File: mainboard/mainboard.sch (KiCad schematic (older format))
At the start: 96 parts, among them J1 USB_B_Micro, J2 Conn_01x19_MountingPin, J3 Conn_01x19_MountingPin, J4 Conn_01x02_Male, Q1 DMG2301L, Q2 MMBT3904, Q3 MMBT3904, SW1 SW_Push, SW2 SW_Push, U1 ESP32-WROOM-32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

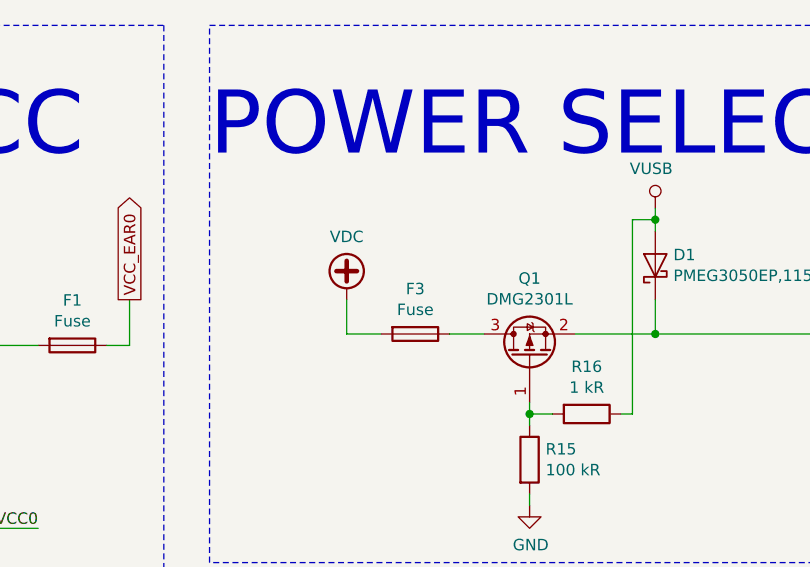
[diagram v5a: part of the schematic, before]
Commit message: Add right-angle XT30 power connector
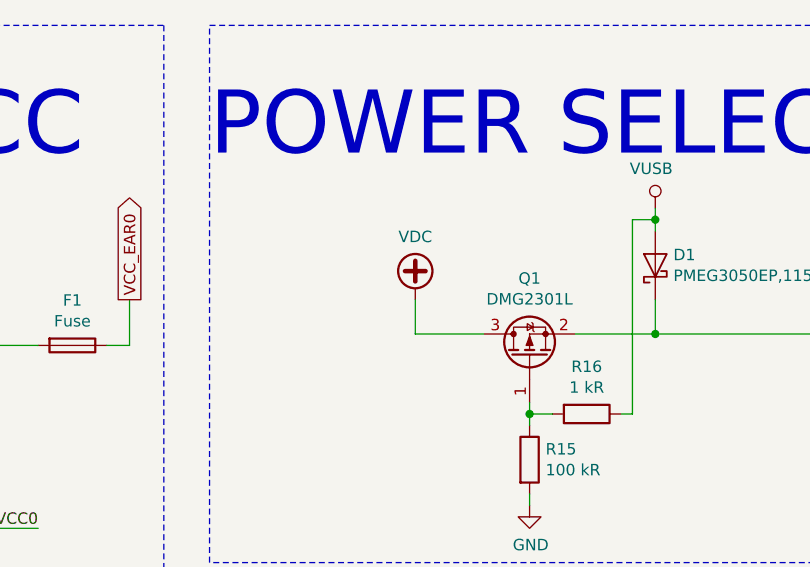
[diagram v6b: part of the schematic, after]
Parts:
- removed F3: Fuse, Fuse:Fuse_0805_2012Metric, symbol Device:Fuse
- F4: footprint Fuse:Fuse_0805_2012Metric -> Fuse:Fuse_1206_3216Metric
- J4: footprint (none) -> mainboard:XT30PW
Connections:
- net VDC: now also Q1.3 (D)
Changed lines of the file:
@@
 L power:VDC #PWR0119
 U 1 1 5D52A44C
-P 7450 5100
-F 0 "#PWR0119" H 7450 5000 50  0001 C CNN
-F 1 "VDC" H 7450 5375 50  0000 C CNN
-F 2 "" H 7450 5100 50  0001 C CNN
-F 3 "" H 7450 5100 50  0001 C CNN
-	1    7450 5100
+P 7750 5100
+F 0 "#PWR0119" H 7750 5000 50  0001 C CNN
+F 1 "VDC" H 7750 5375 50  0000 C CNN
+F 2 "" H 7750 5100 50  0001 C CNN
+F 3 "" H 7750 5100 50  0001 C CNN
+	1    7750 5100
 	1    0    0    -1
 $EndComp
@@
 Wire Wire Line
 	7000 7350 7350 7350
-$Comp
-L Device:Fuse F3
-U 1 1 5EE0ACB2
-P 7750 5250
-F 0 "F3" V 7553 5250 50  0000 C CNN
-F 1 "Fuse" V 7644 5250 50  0000 C CNN
-F 2 "Fuse:Fuse_0805_2012Metric" V 7680 5250 50  0001 C CNN
-F 3 "~" H 7750 5250 50  0001 C CNN
-	1    7750 5250
-	0    1    1    0
-$EndComp
-Wire Wire Line
-	7900 5250 8050 5250
-Wire Wire Line
-	7450 5100 7450 5250
-Wire Wire Line
-	7450 5250 7600 5250
+Wire Wire Line
+	7750 5100 7750 5250
 Wire Wire Line
 	17600 1950 17600 2250
@@
 F 0 "F4" V 14103 4750 50  0000 C CNN
 F 1 "Fuse" V 14194 4750 50  0000 C CNN
-F 2 "Fuse:Fuse_0805_2012Metric" V 14230 4750 50  0001 C CNN
+F 2 "Fuse:Fuse_1206_3216Metric" V 14230 4750 50  0001 C CNN
 F 3 "~" H 14300 4750 50  0001 C CNN
 	1    14300 4750
@@
 F 0 "J4" H 13858 4931 50  0000 C CNN
 F 1 "Conn_01x02_Male" H 13858 4840 50  0000 C CNN
-F 2 "" H 13750 4750 50  0001 C CNN
+F 2 "mainboard:XT30PW" H 13750 4750 50  0001 C CNN
 F 3 "~" H 13750 4750 50  0001 C CNN
 	1    13750 4750
@@
 Text Notes 13700 4300 0    276  ~ 0
 VDC
+Wire Wire Line
+	7750 5250 8050 5250
 Wire Bus Line
 	8350 2150 8350 2500

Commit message: More WIP
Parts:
- removed JP1, JP2, JP3: Jumper_3_Bridged12, Jumper:SolderJumper-3_P1.3mm_Bridged12_Pad1.0x1.5mm, symbol Jumper:Jumper_3_Bridged12
- added C44: 1 uC, Capacitor_SMD:C_0805_2012Metric, symbol Device:C
- added D3, D4, D5, D6, D7, D8, D9: LED, LED_SMD:LED_0805_2012Metric, symbol Device:LED
- added R23, R25: 1 kR, Resistor_SMD:R_0805_2012Metric, symbol Device:R
- added R24: 330 R, Resistor_SMD:R_0805_2012Metric, symbol Device:R
- added R26, R29: 220 R, Resistor_SMD:R_0805_2012Metric, symbol Device:R
- added R27, R28: 470 R, Resistor_SMD:R_0805_2012Metric, symbol Device:R
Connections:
- net +3V3: now also C44.1, D6.2 (A)
- net GND: now also U6.5 (SDO), U7.2 (ADDR), U8.9 (SDO/SA1), C44.2, R23.2, R24.2, R25.2, R26.2, R27.2, R28.2, R29.2
- net VBUS: now also D5.2 (A)
- net VCC_EAR0: now also D7.2 (A)
- net VCC_EAR1: now also D8.2 (A)
- net VDC: now also D3.2 (A)
- net VUSB: now also D4.2 (A)
- net IO4: now reaches U1.26 (IO4)
- net IO4: now also D9.2 (A)
- new net: D3.1 (K), R23.1
- new net: D4.1 (K), R24.1
- new net: D5.1 (K), R25.1
- new net: D6.1 (K), R26.1
- new net: D7.1 (K), R27.1
- new net: D8.1 (K), R28.1
- new net: D9.1 (K), R29.1
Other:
- note added: "LEDs"
- moved on the sheet: C41, C42, U8

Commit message: Finish basic routing
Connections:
- net +3V3: now also R26.1, U6.5 (SDO); no longer D6.2 (A)
- net GND: now also D5.1 (K), D6.1 (K); no longer R25.2, R26.2, U6.5 (SDO)
- net VBUS: now also R25.1; no longer D5.2 (A)
- new net: D5.2 (A), R25.2
- new net: D6.2 (A), R26.2
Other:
- moved on the sheet: D5, D6, R25, R26
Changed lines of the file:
@@
 	9200 10100 9200 9100
 Wire Wire Line
-	9200 9100 8200 9100
+	9200 9100 8800 9100
 Wire Wire Line
 	7250 10550 8000 10550
@@
 L Device:R R25
 U 1 1 5E59E276
-P 17300 4850
-F 0 "R25" H 17370 4896 50  0000 L CNN
-F 1 "1 kR" H 17370 4805 50  0000 L CNN
-F 2 "Resistor_SMD:R_0805_2012Metric" V 17230 4850 50  0001 C CNN
-F 3 "~" H 17300 4850 50  0001 C CNN
-	1    17300 4850
+P 17300 4500
+F 0 "R25" H 17370 4546 50  0000 L CNN
+F 1 "1 kR" H 17370 4455 50  0000 L CNN
+F 2 "Resistor_SMD:R_0805_2012Metric" V 17230 4500 50  0001 C CNN
+F 3 "~" H 17300 4500 50  0001 C CNN
+	1    17300 4500
 	1    0    0    -1
 $EndComp
@@
 F 3 "" H 17800 4200 50  0001 C CNN
 	1    17800 4200
-	1    0    0    -1
-$EndComp
-$Comp
-L Device:R R26
-U 1 1 5E5A0416
-P 17800 4850
-F 0 "R26" H 17870 4896 50  0000 L CNN
-F 1 "220 R" H 17870 4805 50  0000 L CNN
-F 2 "Resistor_SMD:R_0805_2012Metric" V 17730 4850 50  0001 C CNN
-F 3 "~" H 17800 4850 50  0001 C CNN
-	1    17800 4850
 	1    0    0    -1
 $EndComp
@@
 L Device:LED D5
 U 1 1 5E5A26C1
-P 17300 4500
-F 0 "D5" V 17339 4383 50  0000 R CNN
-F 1 "LED" V 17248 4383 50  0000 R CNN
-F 2 "LED_SMD:LED_0805_2012Metric" H 17300 4500 50  0001 C CNN
-F 3 "~" H 17300 4500 50  0001 C CNN
-	1    17300 4500
-	0    -1   -1   0
-$EndComp
-$Comp
-L Device:LED D6
-U 1 1 5E5A377A
-P 17800 4500
-F 0 "D6" V 17839 4383 50  0000 R CNN
-F 1 "LED" V 17748 4383 50  0000 R CNN
-F 2 "LED_SMD:LED_0805_2012Metric" H 17800 4500 50  0001 C CNN
-F 3 "~" H 17800 4500 50  0001 C CNN
-	1    17800 4500
+P 17300 4850
+F 0 "D5" V 17339 4733 50  0000 R CNN
+F 1 "LED" V 17248 4733 50  0000 R CNN
+F 2 "LED_SMD:LED_0805_2012Metric" H 17300 4850 50  0001 C CNN
+F 3 "~" H 17300 4850 50  0001 C CNN
+	1    17300 4850
 	0    -1   -1   0
 $EndComp
@@
 	8700 9500 8800 9500
 Wire Wire Line
-	8800 9500 8800 10550
-Wire Wire Line
-	8800 10550 8200 10550
-Connection ~ 8200 10550
-Wire Wire Line
 	7550 12400 7450 12400
 Wire Wire Line
@@
 	9700 11750 9150 11750
 Connection ~ 9150 11750
+Wire Wire Line
+	8800 9500 8800 9100
 Wire Bus Line
 	8350 2150 8350 2500
 Wire Bus Line
 	9350 2500 9350 2750
+Connection ~ 8800 9100
+Wire Wire Line
+	8800 9100 8200 9100
+$Comp
+L Device:R R26
+U 1 1 5E5A0416
+P 17800 4500
+F 0 "R26" H 17870 4546 50  0000 L CNN
+F 1 "220 R" H 17870 4455 50  0000 L CNN
+F 2 "Resistor_SMD:R_0805_2012Metric" V 17730 4500 50  0001 C CNN
+F 3 "~" H 17800 4500 50  0001 C CNN
+	1    17800 4500
+	1    0    0    -1
+$EndComp
+$Comp
+L Device:LED D6
+U 1 1 5E5A377A
+P 17800 4850
+F 0 "D6" V 17839 4733 50  0000 R CNN
+F 1 "LED" V 17748 4733 50  0000 R CNN
+F 2 "LED_SMD:LED_0805_2012Metric" H 17800 4850 50  0001 C CNN
+F 3 "~" H 17800 4850 50  0001 C CNN
+	1    17800 4850
+	0    -1   -1   0
+$EndComp
 $EndSCHEMATC
